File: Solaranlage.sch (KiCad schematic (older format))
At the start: 111 parts, among them J1 Screw_Terminal_01x02, J2 Screw_Terminal_01x02, J3 AVR-JTAG-10, J4 USB_B, J5 USB_B, J6 Screw_Terminal_01x02, J7 Screw_Terminal_01x02, Q1 2N3904, SW1 Rotary_Encoder_Switch_Panason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, SW2 100SP1T1B4M2QE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

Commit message: created BOM; added ordering codes; changes some footprints; etc.
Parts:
- added BZ1: AL-60SP05/HT, Buzzer_Beeper:Buzzer_12x9.5RM7.6, symbol Device:Buzzer
- added C23: 10uF, Capacitor_THT:CP_Radial_D6.3mm_P2.50mm, symbol Device:CP
- added GND1, GND2: 0, Resistor_THT:R_Axial_DIN0204_L3.6mm_D1.6mm_P7.62mm_Horizontal, symbol Device:R
- added Q2: 2N3904, Package_TO_SOT_THT:TO-92L_Wide, symbol Transistor_BJT:2N3904
- added R35: 1k, Resistor_THT:R_Axial_DIN0204_L3.6mm_D1.6mm_P7.62mm_Horizontal, symbol Device:R
- C1, C15, C20, C5, C6, C8, C9: Ordering (none) -> 1235236-62; Supplier (none) -> Conrad
- C10, C14, C17, C19, C2, C21, C3, C4: footprint Capacitor_THT:C_Disc_D4.7mm_W2.5mm_P5.00mm -> Capacitor_THT:C_Rect_L7.2mm_W2.5mm_P5.00mm_FKS2_FKP2_MKS2_MKP2; Ordering (none) -> 1235240-62; Supplier (none) -> Conrad
- C11, C16, C18: value 13uF -> 10uF; Ordering (none) -> 1688108-62; Supplier (none) -> Conrad
- C12, C13: Ordering (none) -> 1589402-62; Supplier (none) -> Conrad
- C22, C7: footprint Capacitor_THT:C_Rect_L7.0mm_W2.0mm_P5.00mm -> Capacitor_THT:C_Rect_L7.2mm_W2.5mm_P5.00mm_FKS2_FKP2_MKS2_MKP2; Ordering (none) -> 1235240-62; Supplier (none) -> Conrad
- D1: value LED_rot -> LED_red_5mm; Ordering (none) -> 1573740-62; Supplier (none) -> Conrad
- D10, D8, D9: Ordering Conrad: 140823 - 62 -> 140823-62; Supplier (none) -> Conrad
- D11, D14: Ordering Conrad: 140823 - 62 -> 140823 - 62; Supplier (none) -> Conrad
- D12: value K -> LED_yellow_3mm; Ordering Conrad: 1573698 - 62 -> 1573698-62; Supplier (none) -> Conrad
- D13: value M -> LED_yellow_3mm; Ordering Conrad: 1573698 - 62 -> 1573698-62; Supplier (none) -> Conrad
- D2, D3: value LED_gruen -> LED_green_5mm; Ordering (none) -> 1573746-62; Supplier (none) -> Conrad
- D4: value D2 -> LED_yellow_3mm; Ordering Conrad: 1573698 - 62 -> 1573698-62; Supplier (none) -> Conrad
- D5: value D1 -> LED_yellow_3mm; Ordering Conrad: 1573698 - 62 -> 1573698-62; Supplier (none) -> Conrad
- D6: value TK -> LED_yellow_3mm; Ordering Conrad: 1573698 - 62 -> 1573698-62; Supplier (none) -> Conrad
- D7: value TD -> LED_yellow_3mm; Ordering Conrad: 1573698 - 62 -> 1573698-62; Supplier (none) -> Conrad
- F1: footprint fuse:5x20mm -> fuse:696101000002; Ordering (none) -> 1898867-62 / 1898865-62; Supplier (none) -> Conrad
- H5: footprint MountingHole:MountingHole_2.2mm_M2_DIN965_Pad -> MountingHole:MountingHole_3.2mm_M3_DIN965_Pad
- J1, J2, J6: Ordering (none) -> A98092-ND; Supplier (none) -> Digikey
- J3: Ordering Conrad: 1303517 - 62 -> 1088159-62; Supplier (none) -> Conrad
- J4, J5: Ordering Conrad: 1883654-62 -> 1883654-62; Supplier (none) -> Conrad
- J7: Ordering (none) -> A98093-ND; Supplier (none) -> Digikey
- JP1: Ordering (none) -> 739443-62 / MPE 087-1-020; Supplier (none) -> Conrad
- L1, L2, L3: Ordering (none) -> 440313-62; Supplier (none) -> Conrad
- MECH1, MECH2: Ordering Conrad: 189600 - 62 -> 189600-62; Supplier (none) -> Conrad
- MECH3, MECH4: Ordering Conrad: 89626 - 62 -> 89626-62; Supplier (none) -> Conrad
- MECH5: Ordering Conrad: 183839 - 62 -> 183839-62; Supplier (none) -> Conrad
- Q1: Ordering (none) -> 2N 3904; Supplier (none) -> Reichelt
- R1, R12, R13, R19, R2, R21, R23: Ordering (none) -> VIS C1001FC100; Supplier (none) -> Reichelt
- R10, R3, R4, R5, R6, R7, R8, R9: Ordering (none) -> YAG FTE52-220R; Supplier (none) -> Reichelt
- R11, R14, R15, R16, R22, R24, R29, R30, R34: Ordering (none) -> METALL 10,0K; Supplier (none) -> Reichelt
- R17, R18, R20: Ordering (none) -> YAG FTE52-560R; Supplier (none) -> Reichelt
- R25, R26, R27, R28, R31, R32: Ordering (none) -> METALL 330; Supplier (none) -> Reichelt
- R33: Ordering (none) -> VIS C4701FC100; Supplier (none) -> Reichelt
- RV1, RV2: Ordering (none) -> 447564-62; Supplier (none) -> Conrad
- SW1: Ordering Digikey: P12423-ND -> P12423-ND; Supplier (none) -> Digikey
- SW2: Ordering Digikey: EG2355-ND -> EG2355-ND; Supplier (none) -> Digikey
- U1, U2, U3, U4, U5, U6: Ordering Reichelt: C 56-11 RT -> C 56-11 RT; Supplier (none) -> Reichelt
- U10: Ordering (none) -> NE 555 TEX; Supplier (none) -> Reichelt
- U11: Ordering (none) -> LS 126; Supplier (none) -> Reichelt
- U12: Ordering Reichel: 74HC 595 -> 74HC 595; Supplier (none) -> Reichelt
- U7: Ordering Conrad: 812265799 - 62 -> 812265799-62; Supplier (none) -> Conrad
- U8: Ordering (none) -> FT 232 RL; Supplier (none) -> Reichelt
- U9: Ordering Conrad: 651489 - 62 -> 651489-62; Supplier (none) -> Conrad
- Y1: Ordering (none) -> 7,3728-HC49U-S; Supplier (none) -> Reichelt
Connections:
- net +5V: now also BZ1.1 (-)
- net GND: now also C23.2, GND1.1, GND1.2, GND2.1, GND2.2, Q2.1 (E)
- net at L3.1, SW2.1 (A): now also C23.1
- net at U12.6 (QG): now also R35.2
- new net: BZ1.2 (+), Q2.3 (C)
- new net: Q2.2 (B), R35.1
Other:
- note added: "D1"
- note added: "D2"
- note added: "I_max != 500 mA"
- note added: "I_max: 680 mA"
- note added: "K\n"
- note added: "M/A\n"
- note added: "M3, next to encoder\n\n"
- note added: "TD"
- note added: "TK"
- note added: "TODO: 1mA leakage current of TVS diodes at 5,8V semms to be a Problem.\nChose 13V types? Their leakage current would be 1 uA"
- note added: "heartbeat"
- note added: "power"
- note added: "pump"
- note removed: "M2, next to encoder\n\n"
- moved on the sheet: C1, C10, C11, C12, C13, C14, C15, C16, C17, C18, C19, C2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

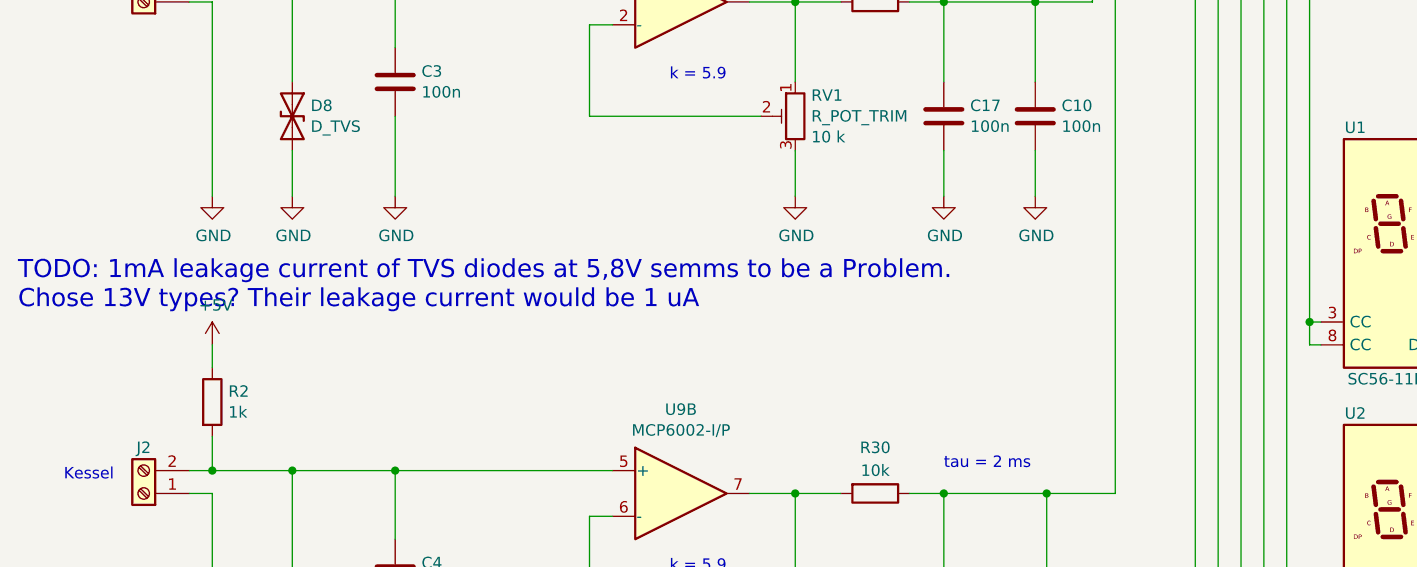
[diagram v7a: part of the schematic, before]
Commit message: replaced TVS diodes by diodes with higher breakdown voltage to minimize leakage current
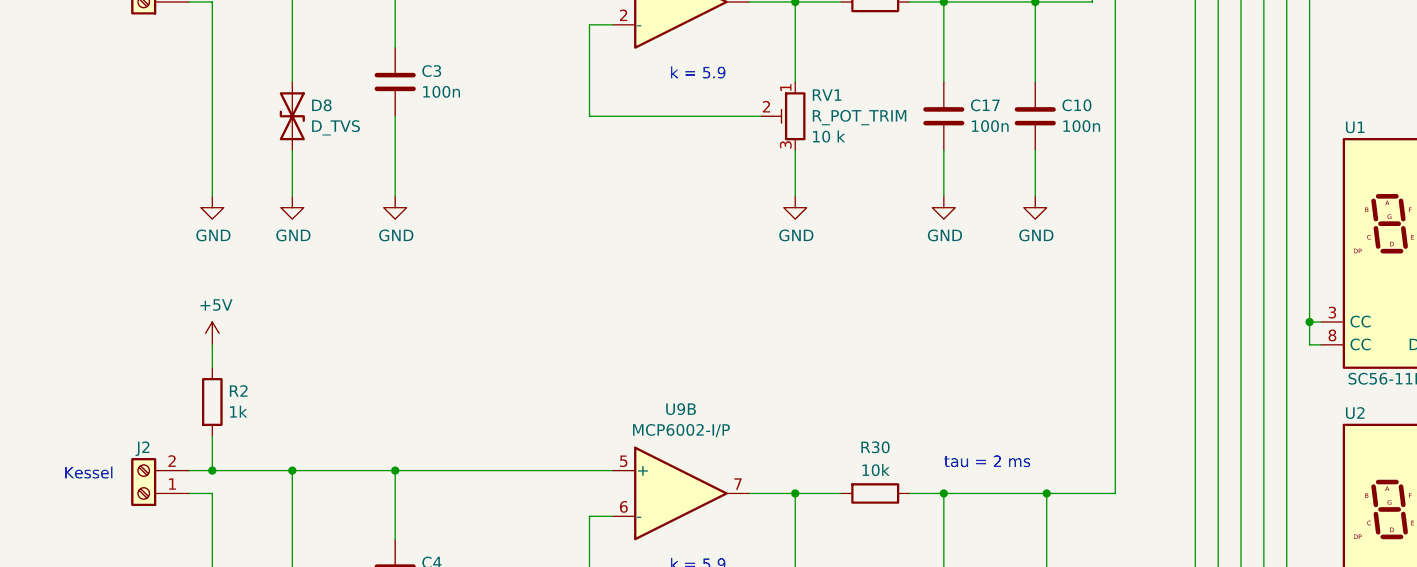
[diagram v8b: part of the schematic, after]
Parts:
- D10, D8, D9: Ordering 140823-62 -> 140810-62
- D11, D14: Ordering 140823 - 62 -> 140810-62
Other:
- note removed: "TODO: 1mA leakage current of TVS diodes at 5,8V semms to be a Problem.\nChose 13V types? Their leakage current would be 1 uA"
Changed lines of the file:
@@
 F 2 "Diode_THT:D_DO-201_P3.81mm_Vertical_KathodeUp" H 6750 13450 50  0001 C CNN
 F 3 "${KIPRJMOD}\\datasheets\\TVS_P6KE6.8A.pdf" H 6750 13450 50  0001 C CNN
-F 4 "140823 - 62" V 6750 13450 50  0001 C CNN "Ordering"
+F 4 "140810-62" V 6750 13450 50  0001 C CNN "Ordering"
 F 5 "Conrad" V 6750 13450 50  0001 C CNN "Supplier"
 	1    6750 13450
@@
 F 2 "Diode_THT:D_DO-201_P3.81mm_Vertical_KathodeUp" H 1750 4500 50  0001 C CNN
 F 3 "${KIPRJMOD}\\datasheets\\TVS_P6KE6.8A.pdf" H 1750 4500 50  0001 C CNN
-F 4 "140823-62" V 1750 4500 50  0001 C CNN "Ordering"
+F 4 "140810-62" V 1750 4500 50  0001 C CNN "Ordering"
 F 5 "Conrad" V 1750 4500 50  0001 C CNN "Supplier"
 	1    1750 4500
@@
 F 2 "Diode_THT:D_DO-201_P3.81mm_Vertical_KathodeUp" H 1750 6650 50  0001 C CNN
 F 3 "${KIPRJMOD}\\datasheets\\TVS_P6KE6.8A.pdf" H 1750 6650 50  0001 C CNN
-F 4 "140823-62" V 1750 6650 50  0001 C CNN "Ordering"
+F 4 "140810-62" V 1750 6650 50  0001 C CNN "Ordering"
 F 5 "Conrad" V 1750 6650 50  0001 C CNN "Supplier"
 	1    1750 6650
@@
 F 2 "Diode_THT:D_DO-201_P3.81mm_Vertical_KathodeUp" H 9350 10100 50  0001 C CNN
 F 3 "${KIPRJMOD}\\datasheets\\TVS_P6KE6.8A.pdf" H 9350 10100 50  0001 C CNN
-F 4 "140823-62" V 9350 10100 50  0001 C CNN "Ordering"
+F 4 "140810-62" V 9350 10100 50  0001 C CNN "Ordering"
 F 5 "Conrad" V 9350 10100 50  0001 C CNN "Supplier"
 	1    9350 10100
@@
 F 2 "Diode_THT:D_DO-201_P3.81mm_Vertical_KathodeUp" H 10500 7050 50  0001 C CNN
 F 3 "${KIPRJMOD}\\datasheets\\TVS_P6KE6.8A.pdf" H 10500 7050 50  0001 C CNN
-F 4 "140823 - 62" V 10500 7050 50  0001 C CNN "Ordering"
+F 4 "140810-62" V 10500 7050 50  0001 C CNN "Ordering"
 F 5 "Conrad" V 10500 7050 50  0001 C CNN "Supplier"
 	1    10500 7050
@@
 	1    0    0    -1
 $EndComp
-Text Notes 550  5350 0    79   ~ 0
-TODO: 1mA leakage current of TVS diodes at 5,8V semms to be a Problem.\nChose 13V types? Their leakage current would be 1 uA
 $EndSCHEMATC
